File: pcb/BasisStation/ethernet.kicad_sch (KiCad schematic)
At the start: 35 parts, among them T1 7499011121A, U7 W5500, Y1 25 MHz

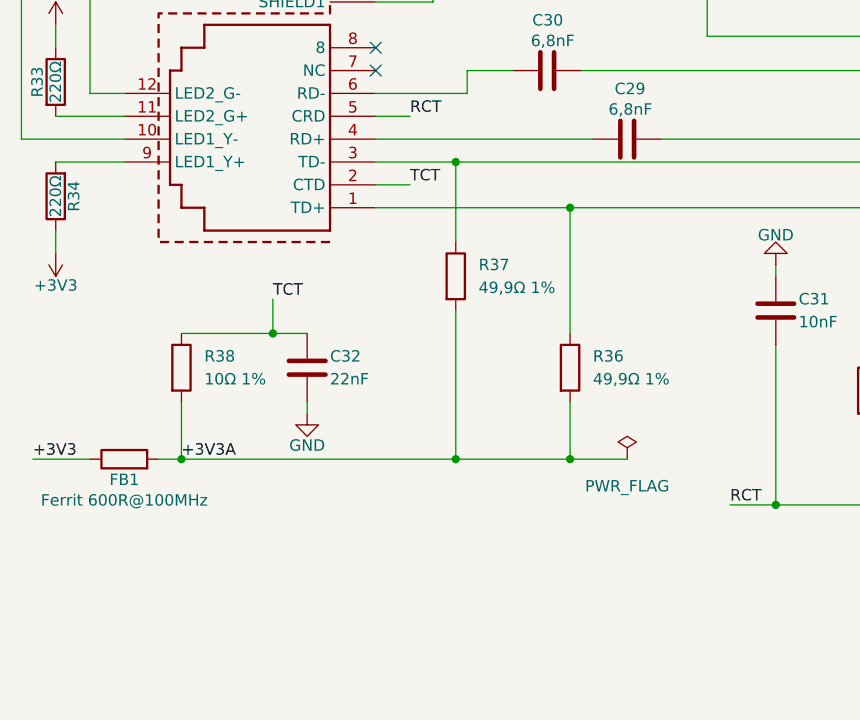
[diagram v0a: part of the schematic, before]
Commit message: v0.00.001 fix(SHBS-5): Footprints ergaenzt, drawio-Diagramm gestrichen
Die BOM-Auswertung zeigte 13 Kondensatoren ohne Footprint - C16 bis C28.
Ohne Footprint landen sie beim Uebertragen der Netzliste nicht auf dem
Board. Alle auf Capacitor_SMD:C_0805_2012Metric gesetzt, ausser C28: Der
bekommt wegen der 2 kV vorlaeufig 1206, endgueltig nach Auswahl des Typs.
Damit tragen alle 35 Bauteile des Ethernet-Blatts einen Footprint.

Das drawio-Architekturdiagramm wurde gestrichen. Es lag in drei Dateien
vor, war an vier Stellen veraltet - +24V, USB-UART-Bridge, JTAG-Header
und fehlendes Ethernet - und duplizierte das Textdiagramm in
architecture.md, das versioniert und im Diff sichtbar ist. Der Verweis in
hardware.md zeigt jetzt dorthin.

Co-Authored-By: Claude Opus 5 <noreply@anthropic.com>
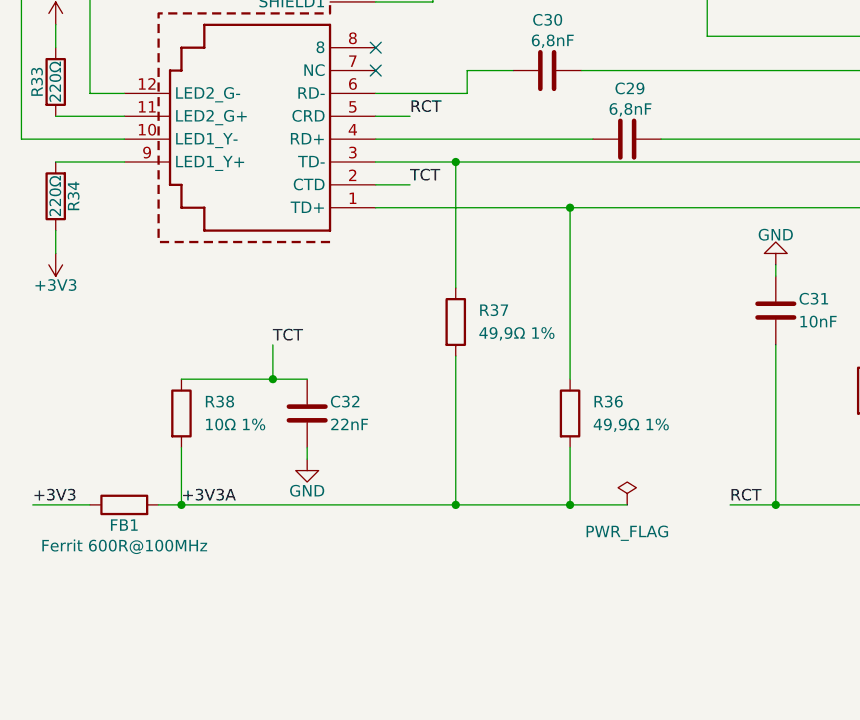
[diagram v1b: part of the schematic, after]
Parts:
- C16, C17, C18, C19, C20, C21, C22, C23, C24, C25, C26, C27: footprint (none) -> Capacitor_SMD:C_0805_2012Metric
- C28: footprint (none) -> Capacitor_SMD:C_1206_3216Metric
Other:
- moved on the sheet: C32, FB1, R36, R37, R38
